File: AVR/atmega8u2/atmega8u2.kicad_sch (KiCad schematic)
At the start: 13 parts

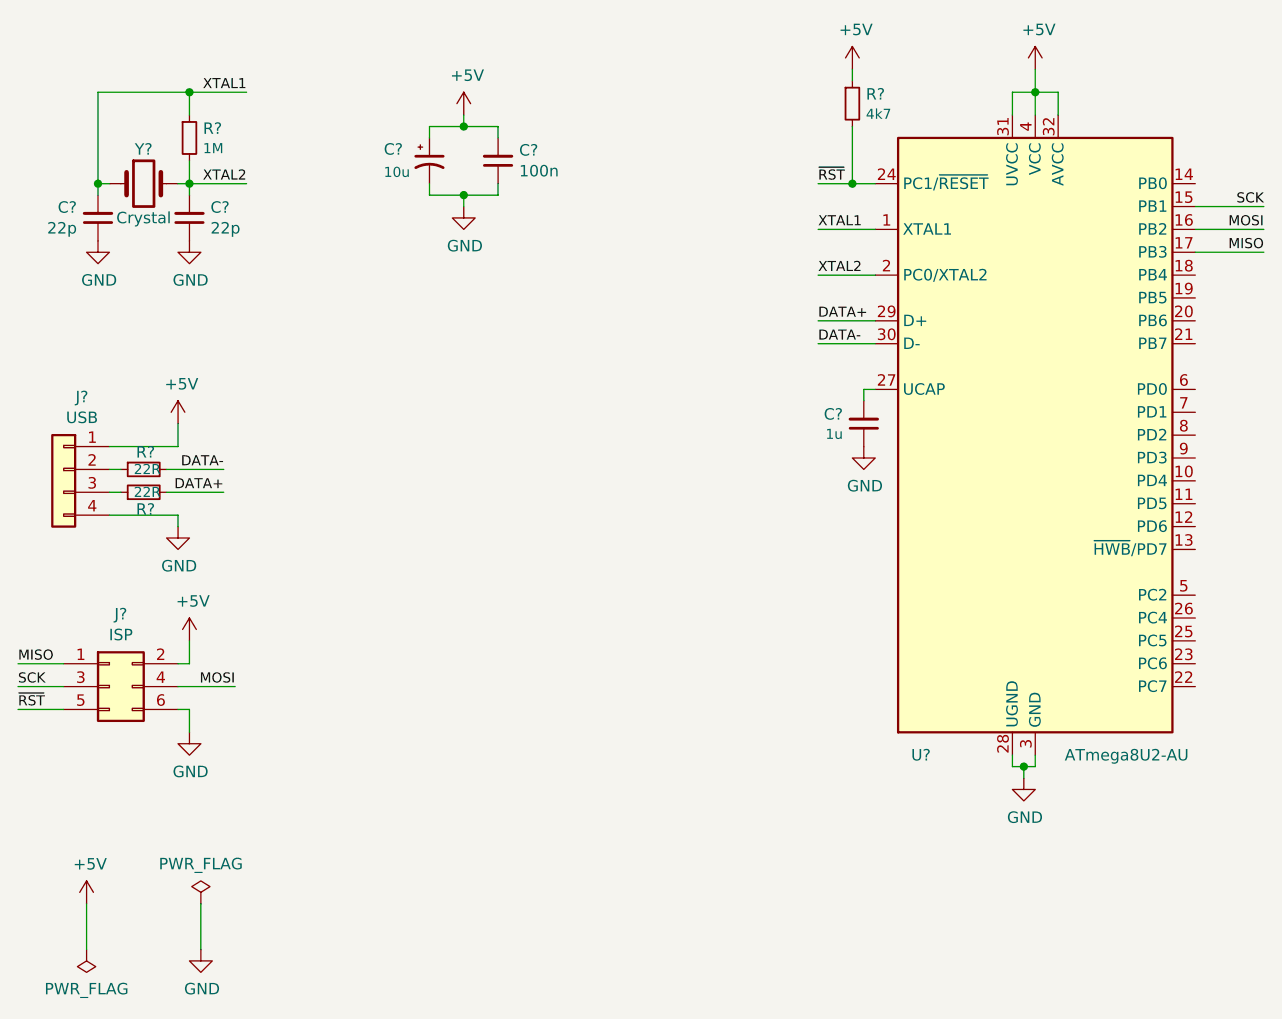
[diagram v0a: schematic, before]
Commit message: Fix grid alignment and update to KiCad 9
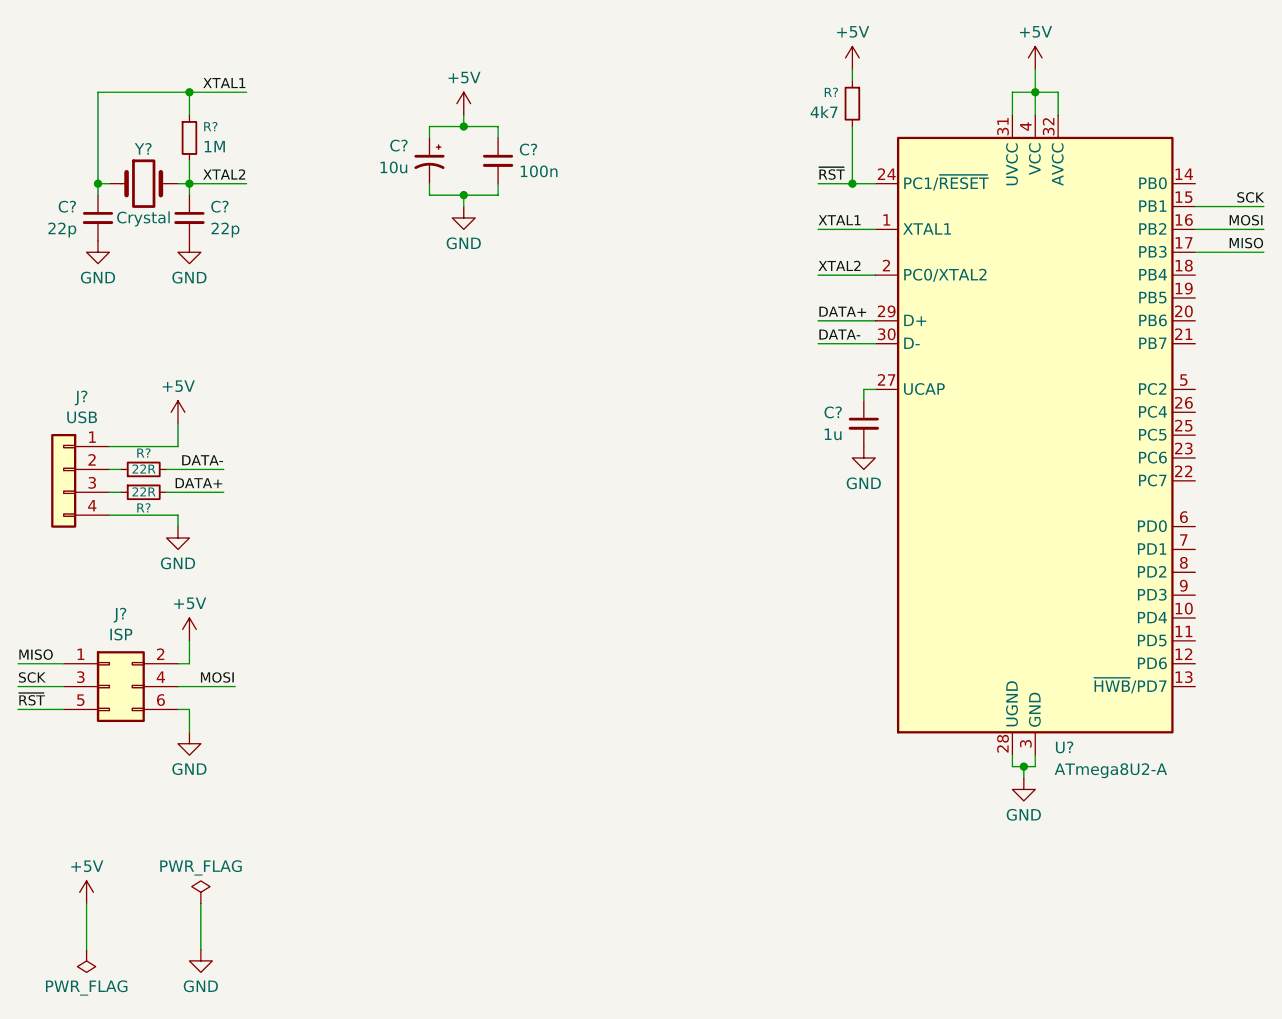
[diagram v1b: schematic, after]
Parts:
- removed C? (x2): 22p, symbol Device:C_Small
- removed C?: 1u, symbol Device:C_Small
- removed C?: 100n, symbol Device:C_Small
- removed C?: 10u, symbol Device:CP1_Small
- removed R?: 1M, symbol Device:R_Small
- removed R?: 4k7, symbol Device:R_Small
- removed R? (x2): 22R, symbol Device:R_Small
- removed U?: ATmega8U2-AU, Package_QFP:TQFP-32_7x7mm_P0.8mm, symbol atmega8u2-rescue:ATmega8U2-AU-MCU_Microchip_ATmega
- added C? (x2): 22p, symbol Device:C_Small
- added C?: 1u, symbol Device:C_Small
- added C?: 10u, symbol Device:C_Polarized_Small_US
- added C?: 100n, symbol Device:C_Small
- added R? (x2): 22R, symbol Device:R_Small
- added R?: 1M, symbol Device:R_Small
- added R?: 4k7, symbol Device:R_Small
- added U?: ATmega8U2-A, Package_QFP:TQFP-32_7x7mm_P0.8mm, symbol MCU_Microchip_ATmega:ATmega8U2-A
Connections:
- net +5V: now also C?.1, C?.1, R?.1, U?.31 (UVCC), U?.32 (AVCC), U?.4 (VCC)
- net DATA+: now also R?.2, U?.29 (D+)
- net DATA-: now also R?.2, U?.30 (D-)
- net GND: now also C?.2, C?.2, C?.2, C?.2, C?.2, U?.28 (UGND), U?.3 (GND)
- net MISO: now also U?.17 (PB3)
- net MOSI: now also U?.16 (PB2)
- net SCK: now also U?.15 (PB1)
- net XTAL1: now also C?.1, R?.1, U?.1 (XTAL1)
- net XTAL2: now also C?.1, R?.2, U?.2 (PC0/XTAL2)
- net ~{RST}: now also R?.2, U?.24 (PC1/~{RESET})
- net at J?.2 (Pin_2): now also R?.1
- net at J?.3 (Pin_3): now also R?.1
- new net: C?.1, U?.27 (UCAP)
